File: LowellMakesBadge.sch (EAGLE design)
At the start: 2 parts

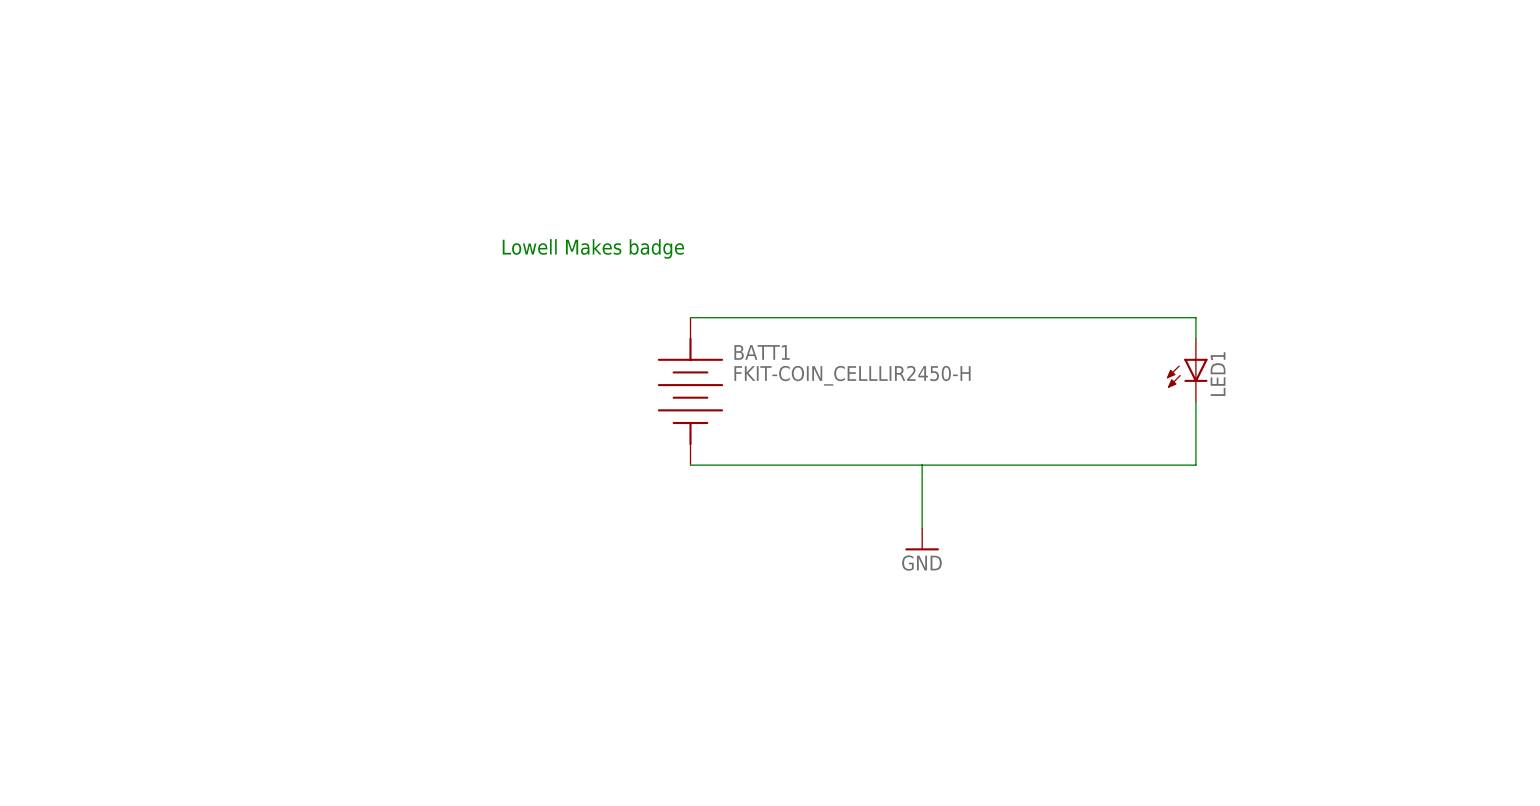
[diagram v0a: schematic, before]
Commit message: Adding next version from @sajingeo including a 3d model
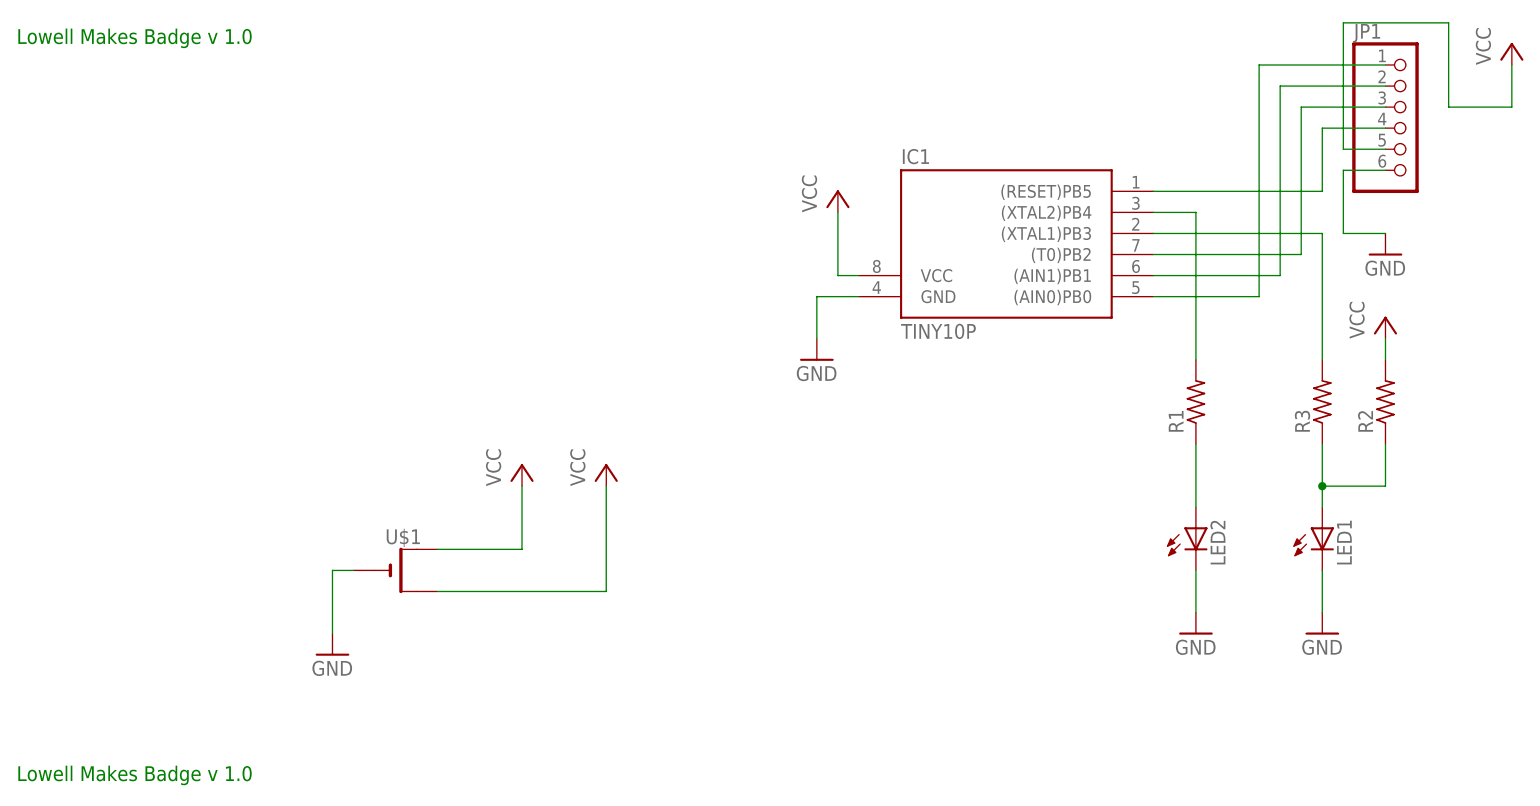
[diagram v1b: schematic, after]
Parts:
- removed BATT1: FKIT-COIN_CELLLIR2450-H, SparkFun-Electromechanical:FKIT-COIN_CELLLIR2450-H
- added IC1: TINY10P, atmel:TINY10P
- added JP1: (no value), adafruit:PINHD-1X6
- added LED2: (no value), adafruit:LED5MM
- added R1, R3: (no value), adafruit:R-US_0204/7
- added R2: (no value), adafruit:R-US_R0603
- added U$1: (no value), adafruit:CR2032THM
- LED1: device led:LED5MM -> adafruit:LED5MM
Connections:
- removed net N$1: BATT1.POS, LED1.A
- new net N$2: LED2.A, R1.1
- new net N$3: IC1.(XTAL1)PB3, R3.2
- new net N$4: LED1.A, R2.1, R3.1
- new net N$5: IC1.(XTAL2)PB4, R1.2
- new net N$6: IC1.(AIN0)PB0, JP1.1
- new net N$7: IC1.(AIN1)PB1, JP1.2
- new net N$8: IC1.(T0)PB2, JP1.3
- new net N$9: IC1.(RESET)PB5, JP1.4
- new net VCC: IC1.VCC, JP1.5, R2.2, U$1.+, U$1.+1
- net GND: now also IC1.GND, JP1.6, LED2.C, U$1.-; no longer BATT1.NEG
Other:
- note added: "Lowell Makes Badge v 1.0"
- note removed: "Lowell Makes badge"
- moved on the sheet: LED1

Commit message: More updates from @sajingeo
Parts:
- IC1: value TINY10P -> TINY10S; device atmel:TINY10P -> atmel:TINY10S
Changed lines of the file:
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@@
 <grid distance="0.1" unitdist="inch" unit="inch" style="lines" multiple="1" display="no" altdistance="0.01" altunitdist="inch" altunit="inch"/>
 <layers>
-<layer number="1" name="Top" color="4" fill="1" visible="no" active="no"/>
-<layer number="16" name="Bottom" color="1" fill="1" visible="no" active="no"/>
-<layer number="17" name="Pads" color="2" fill="1" visible="no" active="no"/>
-<layer number="18" name="Vias" color="2" fill="1" visible="no" active="no"/>
-<layer number="19" name="Unrouted" color="6" fill="1" visible="no" active="no"/>
-<layer number="20" name="Dimension" color="15" fill="1" visible="no" active="no"/>
-<layer number="21" name="tPlace" color="7" fill="1" visible="no" active="no"/>
-<layer number="22" name="bPlace" color="7" fill="1" visible="no" active="no"/>
-<layer number="23" name="tOrigins" color="15" fill="1" visible="no" active="no"/>
-<layer number="24" name="bOrigins" color="15" fill="1" visible="no" active="no"/>
-<layer number="25" name="tNames" color="7" fill="1" visible="no" active="no"/>
-<layer number="26" name="bNames" color="7" fill="1" visible="no" active="no"/>
-<layer number="27" name="tValues" color="7" fill="1" visible="no" active="no"/>
-<layer number="28" name="bValues" color="7" fill="1" visible="no" active="no"/>
+<layer number="1" name="Top" color="4" fill="1" visible="yes" active="no"/>
+<layer number="16" name="Bottom" color="1" fill="1" visible="yes" active="no"/>
+<layer number="17" name="Pads" color="2" fill="1" visible="yes" active="no"/>
+<layer number="18" name="Vias" color="2" fill="1" visible="yes" active="no"/>
+<layer number="19" name="Unrouted" color="6" fill="1" visible="yes" active="no"/>
+<layer number="20" name="Dimension" color="15" fill="1" visible="yes" active="no"/>
+<layer number="21" name="tPlace" color="7" fill="1" visible="yes" active="no"/>
+<layer number="22" name="bPlace" color="7" fill="1" visible="yes" active="no"/>
+<layer number="23" name="tOrigins" color="15" fill="1" visible="yes" active="no"/>
+<layer number="24" name="bOrigins" color="15" fill="1" visible="yes" active="no"/>
+<layer number="25" name="tNames" color="7" fill="1" visible="yes" active="no"/>
+<layer number="26" name="bNames" color="7" fill="1" visible="yes" active="no"/>
+<layer number="27" name="tValues" color="7" fill="1" visible="yes" active="no"/>
+<layer number="28" name="bValues" color="7" fill="1" visible="yes" active="no"/>
 <layer number="29" name="tStop" color="7" fill="3" visible="no" active="no"/>
 <layer number="30" name="bStop" color="7" fill="6" visible="no" active="no"/>
@@
 <layer number="35" name="tGlue" color="7" fill="4" visible="no" active="no"/>
 <layer number="36" name="bGlue" color="7" fill="5" visible="no" active="no"/>
-<layer number="37" name="tTest" color="7" fill="1" visible="no" active="no"/>
-<layer number="38" name="bTest" color="7" fill="1" visible="no" active="no"/>
+<layer number="37" name="tTest" color="7" fill="1" visible="yes" active="no"/>
+<layer number="38" name="bTest" color="7" fill="1" visible="yes" active="no"/>
 <layer number="39" name="tKeepout" color="4" fill="11" visible="no" active="no"/>
 <layer number="40" name="bKeepout" color="1" fill="11" visible="no" active="no"/>
@@
 <layer number="44" name="Drills" color="7" fill="1" visible="no" active="no"/>
 <layer number="45" name="Holes" color="7" fill="1" visible="no" active="no"/>
-<layer number="46" name="Milling" color="3" fill="1" visible="no" active="no"/>
-<layer number="47" name="Measures" color="7" fill="1" visible="no" active="no"/>
-<layer number="48" name="Document" color="7" fill="1" visible="no" active="no"/>
-<layer number="49" name="Reference" color="7" fill="1" visible="no" active="no"/>
-<layer number="50" name="dxf" color="7" fill="1" visible="no" active="no"/>
-<layer number="51" name="tDocu" color="7" fill="1" visible="no" active="no"/>
-<layer number="52" name="bDocu" color="7" fill="1" visible="no" active="no"/>
-<layer number="53" name="tGND_GNDA" color="7" fill="9" visible="no" active="no"/>
-<layer number="54" name="bGND_GNDA" color="1" fill="9" visible="no" active="no"/>
-<layer number="56" name="wert" color="7" fill="1" visible="no" active="no"/>
-<layer number="57" name="tCAD" color="7" fill="1" visible="no" active="no"/>
+<layer number="46" name="Milling" color="3" fill="1" visible="yes" active="no"/>
+<layer number="47" name="Measures" color="7" fill="1" visible="yes" active="no"/>
+<layer number="48" name="Document" color="7" fill="1" visible="yes" active="no"/>
+<layer number="49" name="Reference" color="7" fill="1" visible="yes" active="no"/>
+<layer number="50" name="dxf" color="7" fill="1" visible="yes" active="no"/>
+<layer number="51" name="tDocu" color="7" fill="1" visible="yes" active="no"/>
+<layer number="52" name="bDocu" color="7" fill="1" visible="yes" active="no"/>
+<layer number="53" name="tGND_GNDA" color="7" fill="9" visible="yes" active="no"/>
+<layer number="54" name="bGND_GNDA" color="1" fill="9" visible="yes" active="no"/>
+<layer number="56" name="wert" color="7" fill="1" visible="yes" active="no"/>
+<layer number="57" name="tCAD" color="7" fill="1" visible="yes" active="no"/>
 <layer number="90" name="Modules" color="5" fill="1" visible="yes" active="yes"/>
 <layer number="91" name="Nets" color="2" fill="1" visible="yes" active="yes"/>
@@
 <part name="LED1" library="adafruit" deviceset="LED" device="5MM"/>
 <part name="U$1" library="adafruit" deviceset="CR2032" device="THM"/>
-<part name="IC1" library="atmel" deviceset="TINY10" device="P"/>
+<part name="IC1" library="atmel" deviceset="TINY10" device="S" value="TINY10S"/>
 <part name="R1" library="adafruit" deviceset="R-US_" device="0204/7"/>
 <part name="LED2" library="adafruit" deviceset="LED" device="5MM"/>

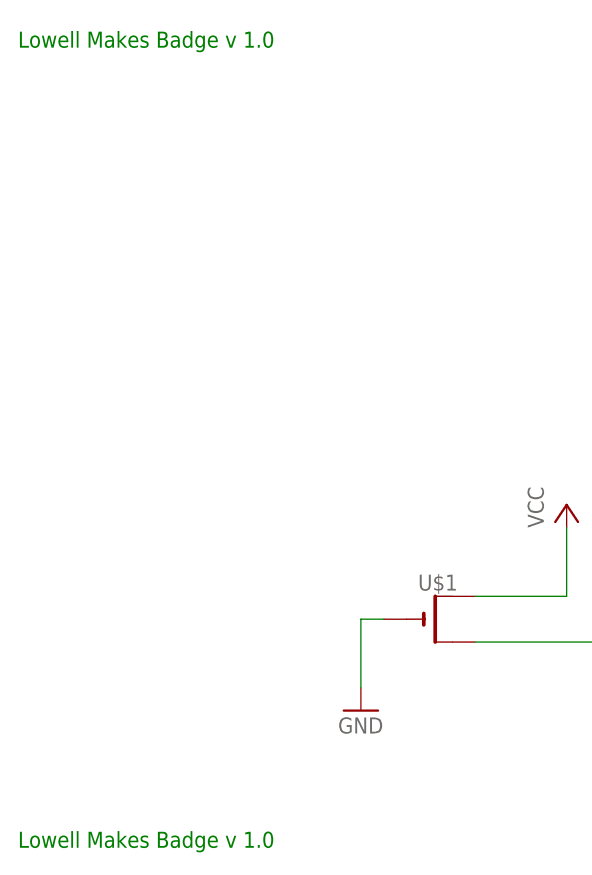
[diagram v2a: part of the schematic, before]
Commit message: Updated board to change version from 1 to 2.0
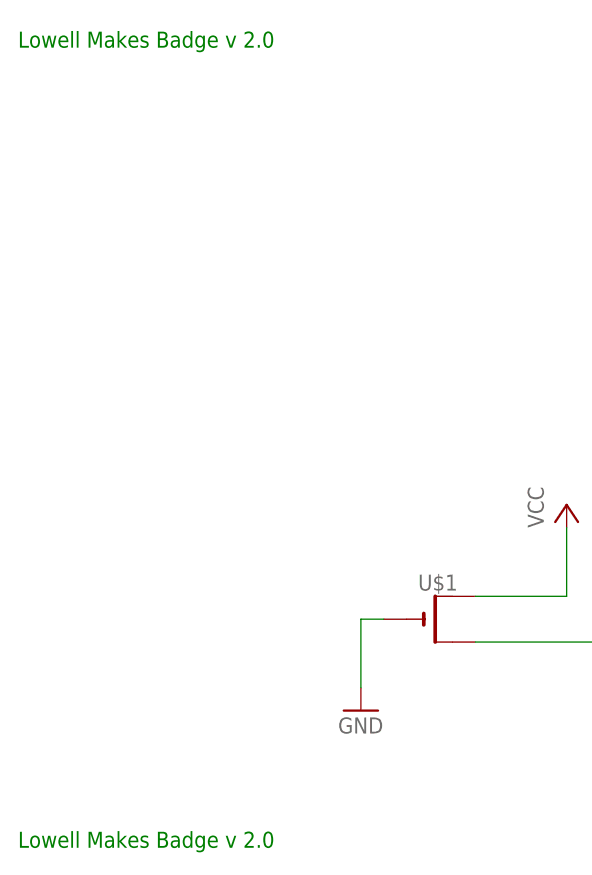
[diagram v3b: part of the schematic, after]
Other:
- note added: "Lowell Makes Badge v 2.0"
- note removed: "Lowell Makes Badge v 1.0"
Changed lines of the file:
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@@
 <grid distance="0.1" unitdist="inch" unit="inch" style="lines" multiple="1" display="no" altdistance="0.01" altunitdist="inch" altunit="inch"/>
 <layers>
-<layer number="1" name="Top" color="4" fill="1" visible="yes" active="no"/>
-<layer number="16" name="Bottom" color="1" fill="1" visible="yes" active="no"/>
-<layer number="17" name="Pads" color="2" fill="1" visible="yes" active="no"/>
-<layer number="18" name="Vias" color="2" fill="1" visible="yes" active="no"/>
-<layer number="19" name="Unrouted" color="6" fill="1" visible="yes" active="no"/>
-<layer number="20" name="Dimension" color="15" fill="1" visible="yes" active="no"/>
-<layer number="21" name="tPlace" color="7" fill="1" visible="yes" active="no"/>
-<layer number="22" name="bPlace" color="7" fill="1" visible="yes" active="no"/>
-<layer number="23" name="tOrigins" color="15" fill="1" visible="yes" active="no"/>
-<layer number="24" name="bOrigins" color="15" fill="1" visible="yes" active="no"/>
-<layer number="25" name="tNames" color="7" fill="1" visible="yes" active="no"/>
-<layer number="26" name="bNames" color="7" fill="1" visible="yes" active="no"/>
-<layer number="27" name="tValues" color="7" fill="1" visible="yes" active="no"/>
-<layer number="28" name="bValues" color="7" fill="1" visible="yes" active="no"/>
+<layer number="1" name="Top" color="4" fill="1" visible="no" active="no"/>
+<layer number="16" name="Bottom" color="1" fill="1" visible="no" active="no"/>
+<layer number="17" name="Pads" color="2" fill="1" visible="no" active="no"/>
+<layer number="18" name="Vias" color="2" fill="1" visible="no" active="no"/>
+<layer number="19" name="Unrouted" color="6" fill="1" visible="no" active="no"/>
+<layer number="20" name="Dimension" color="15" fill="1" visible="no" active="no"/>
+<layer number="21" name="tPlace" color="7" fill="1" visible="no" active="no"/>
+<layer number="22" name="bPlace" color="7" fill="1" visible="no" active="no"/>
+<layer number="23" name="tOrigins" color="15" fill="1" visible="no" active="no"/>
+<layer number="24" name="bOrigins" color="15" fill="1" visible="no" active="no"/>
+<layer number="25" name="tNames" color="7" fill="1" visible="no" active="no"/>
+<layer number="26" name="bNames" color="7" fill="1" visible="no" active="no"/>
+<layer number="27" name="tValues" color="7" fill="1" visible="no" active="no"/>
+<layer number="28" name="bValues" color="7" fill="1" visible="no" active="no"/>
 <layer number="29" name="tStop" color="7" fill="3" visible="no" active="no"/>
 <layer number="30" name="bStop" color="7" fill="6" visible="no" active="no"/>
@@
 <layer number="35" name="tGlue" color="7" fill="4" visible="no" active="no"/>
 <layer number="36" name="bGlue" color="7" fill="5" visible="no" active="no"/>
-<layer number="37" name="tTest" color="7" fill="1" visible="yes" active="no"/>
-<layer number="38" name="bTest" color="7" fill="1" visible="yes" active="no"/>
+<layer number="37" name="tTest" color="7" fill="1" visible="no" active="no"/>
+<layer number="38" name="bTest" color="7" fill="1" visible="no" active="no"/>
 <layer number="39" name="tKeepout" color="4" fill="11" visible="no" active="no"/>
 <layer number="40" name="bKeepout" color="1" fill="11" visible="no" active="no"/>
@@
 <layer number="44" name="Drills" color="7" fill="1" visible="no" active="no"/>
 <layer number="45" name="Holes" color="7" fill="1" visible="no" active="no"/>
-<layer number="46" name="Milling" color="3" fill="1" visible="yes" active="no"/>
-<layer number="47" name="Measures" color="7" fill="1" visible="yes" active="no"/>
-<layer number="48" name="Document" color="7" fill="1" visible="yes" active="no"/>
-<layer number="49" name="Reference" color="7" fill="1" visible="yes" active="no"/>
-<layer number="50" name="dxf" color="7" fill="1" visible="yes" active="no"/>
-<layer number="51" name="tDocu" color="7" fill="1" visible="yes" active="no"/>
-<layer number="52" name="bDocu" color="7" fill="1" visible="yes" active="no"/>
-<layer number="53" name="tGND_GNDA" color="7" fill="9" visible="yes" active="no"/>
-<layer number="54" name="bGND_GNDA" color="1" fill="9" visible="yes" active="no"/>
-<layer number="56" name="wert" color="7" fill="1" visible="yes" active="no"/>
-<layer number="57" name="tCAD" color="7" fill="1" visible="yes" active="no"/>
+<layer number="46" name="Milling" color="3" fill="1" visible="no" active="no"/>
+<layer number="47" name="Measures" color="7" fill="1" visible="no" active="no"/>
+<layer number="48" name="Document" color="7" fill="1" visible="no" active="no"/>
+<layer number="49" name="Reference" color="7" fill="1" visible="no" active="no"/>
+<layer number="50" name="dxf" color="7" fill="1" visible="no" active="no"/>
+<layer number="51" name="tDocu" color="7" fill="1" visible="no" active="no"/>
+<layer number="52" name="bDocu" color="7" fill="1" visible="no" active="no"/>
+<layer number="53" name="tGND_GNDA" color="7" fill="9" visible="no" active="no"/>
+<layer number="54" name="bGND_GNDA" color="1" fill="9" visible="no" active="no"/>
+<layer number="56" name="wert" color="7" fill="1" visible="no" active="no"/>
+<layer number="57" name="tCAD" color="7" fill="1" visible="no" active="no"/>
 <layer number="90" name="Modules" color="5" fill="1" visible="yes" active="yes"/>
 <layer number="91" name="Nets" color="2" fill="1" visible="yes" active="yes"/>
@@
 <sheet>
 <plain>
-<text x="-81.28" y="7.62" size="1.778" layer="91">Lowell Makes Badge v 1.0</text>
-<text x="-81.28" y="96.52" size="1.778" layer="91">Lowell Makes Badge v 1.0</text>
+<text x="-81.28" y="7.62" size="1.778" layer="91">Lowell Makes Badge v 2.0</text>
+<text x="-81.28" y="96.52" size="1.778" layer="91">Lowell Makes Badge v 2.0</text>
 </plain>
 <instances>
